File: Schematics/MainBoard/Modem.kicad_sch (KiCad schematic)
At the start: 27 parts, among them J10 Conn_02x05_Odd_Even, U13 ESP8266-01_ESP-01, U14 AMS1117-3.3, U15 TXS0102DCT, U16 ATmega644P-20A, Y1 ECS-3961-200-AU-TR

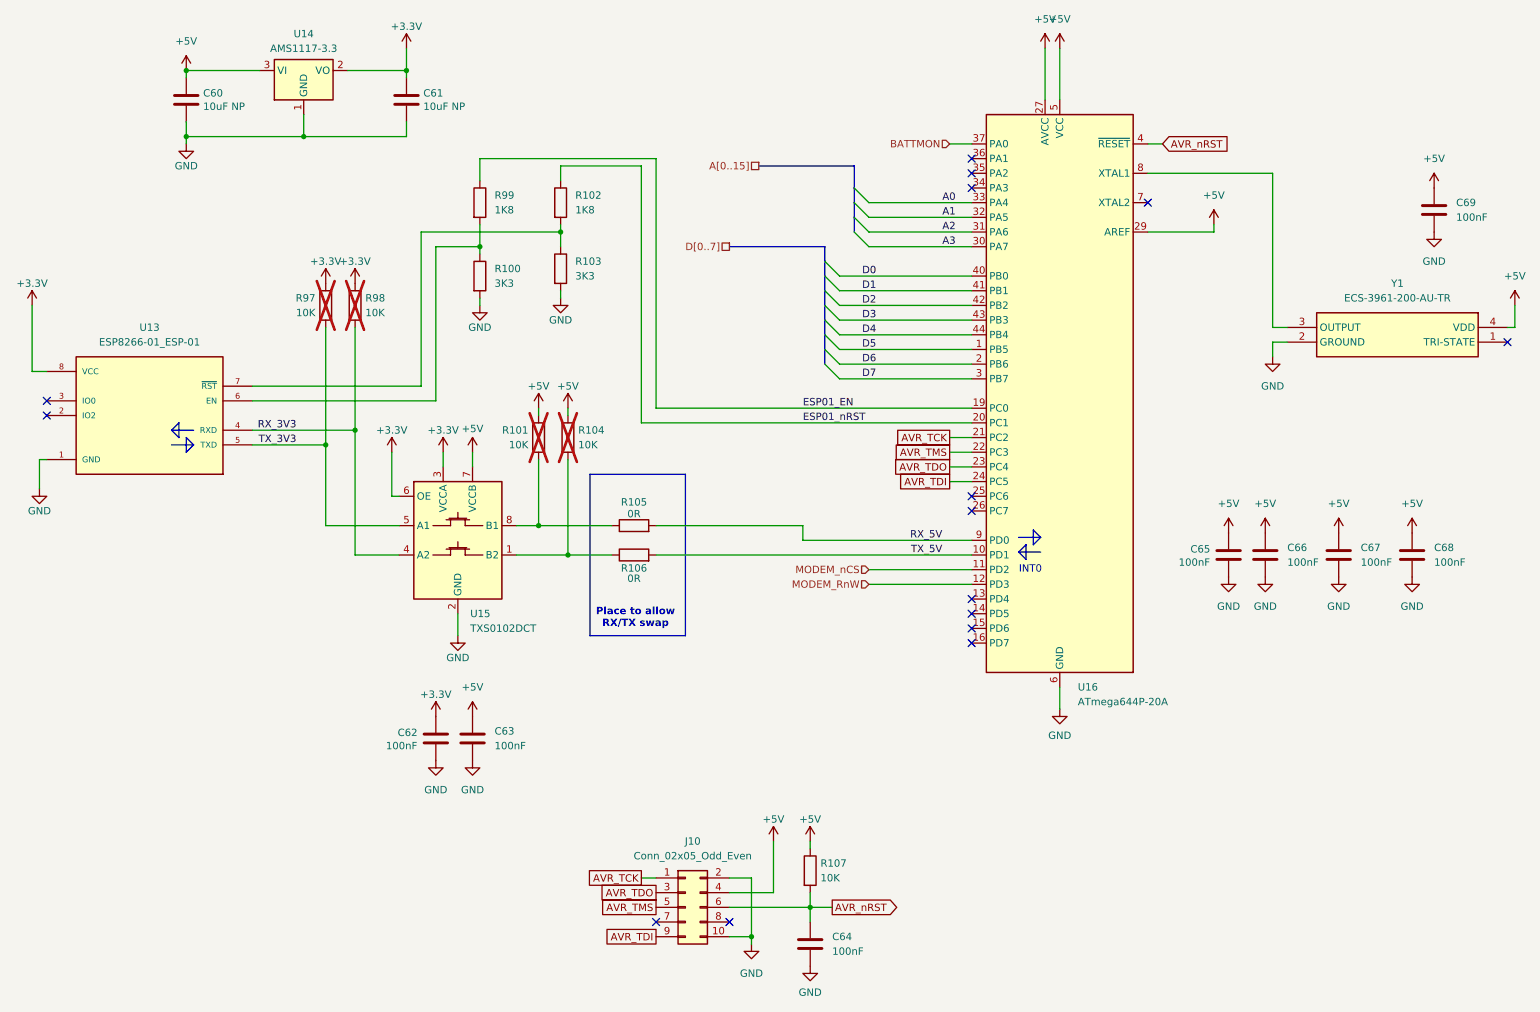
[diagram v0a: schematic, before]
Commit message: Move to a single board for everything (keyboard and main board)
Aim is to save height
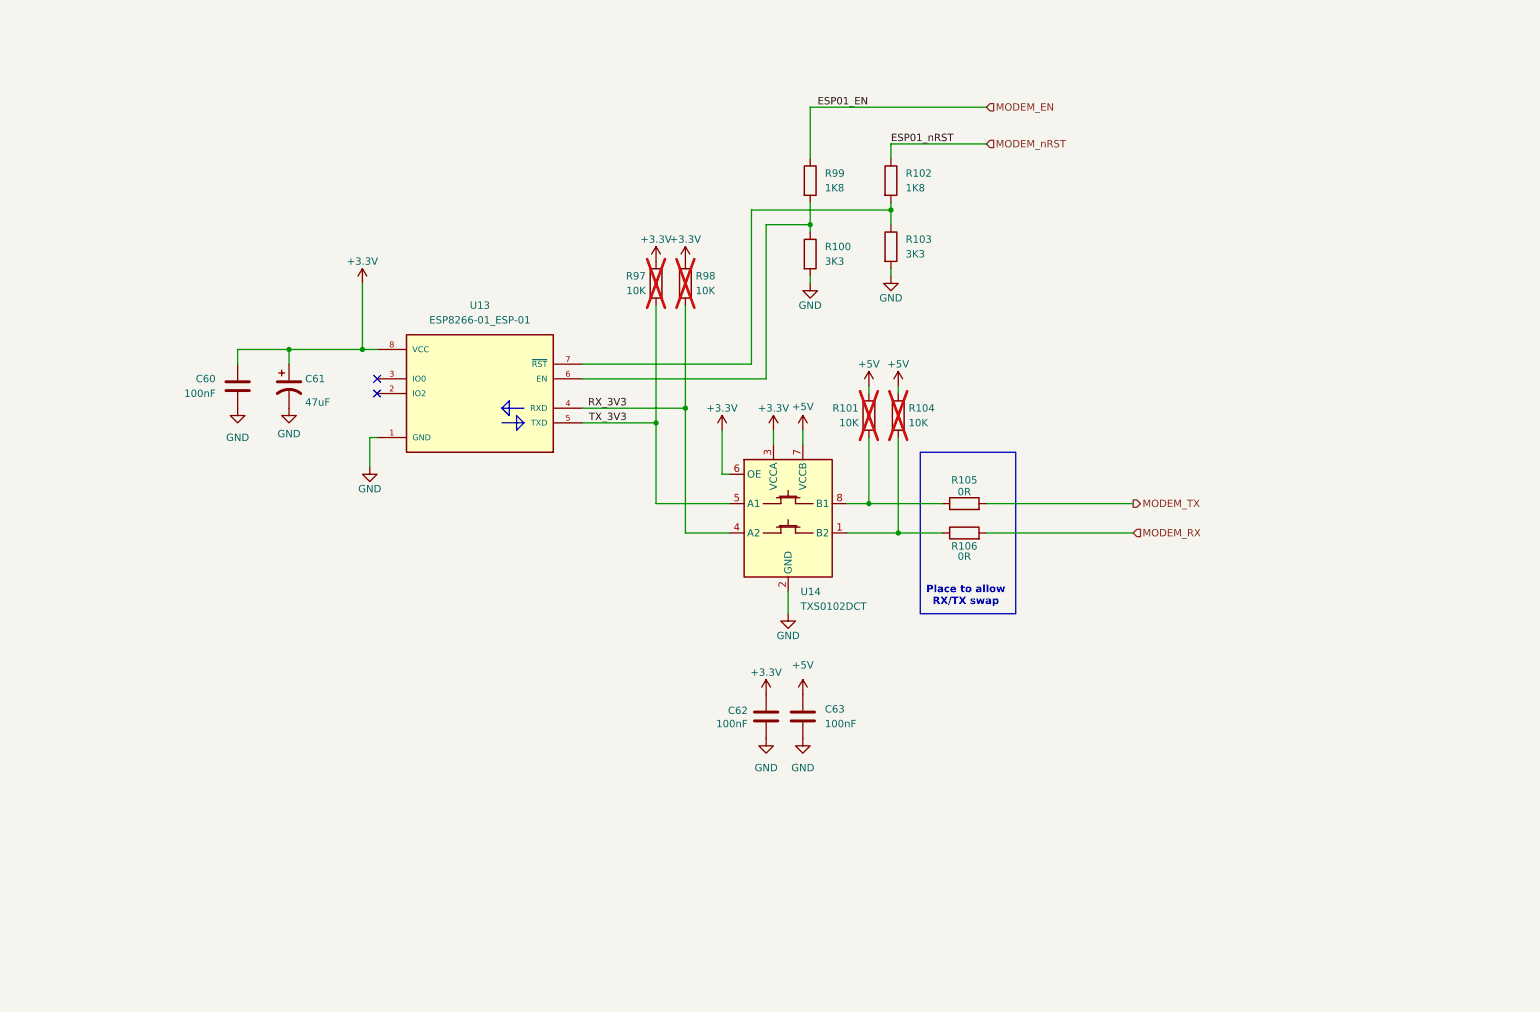
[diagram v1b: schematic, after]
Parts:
- removed C60, C61: 10uF NP, Capacitor_SMD:C_0805_2012Metric, symbol Device:C
- removed C64, C65, C66, C67, C69: 100nF, Capacitor_SMD:C_0402_1005Metric, symbol Device:C
- removed J10: Conn_02x05_Odd_Even, Connector_PinHeader_2.54mm:PinHeader_2x05_P2.54mm_Vertical, symbol Connector_Generic:Conn_02x05_Odd_Even
- removed R107: 10K, Resistor_SMD:R_0402_1005Metric, symbol Device:R
- removed U14: AMS1117-3.3, Package_TO_SOT_SMD:SOT-223-3_TabPin2, symbol Regulator_Linear:AMS1117-3.3
- removed U16: ATmega644P-20A, Package_QFP:TQFP-44_10x10mm_P0.8mm, symbol MCU_Microchip_ATmega:ATmega644P-20A
- removed Y1: ECS-3961-200-AU-TR, ECS-3961-200-AU-TR:ECS3961200AUTR, symbol ECS-3961-200-AU-TR:ECS-3961-200-AU-TR
- added C61: 47uF, Capacitor_SMD:C_1206_3216Metric, symbol Device:C_Polarized_US
- renumbered C68 to C60, U15 to U14
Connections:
- net +3.3V: now also C60.1, C61.1
- net +5V: no longer C60.1
- net GND: now also C61.2
- net ESP01_EN renamed MODEM_EN
- net ESP01_nRST renamed MODEM_nRST
- net RX_5V renamed MODEM_TX
- net TX_5V renamed MODEM_RX
- no-connect marks 15 -> 2
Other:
- note removed: "INT0"
- moved on the sheet: C60, C62, C63, R100, R101, R102, R103, R104, R105, R106, R97, R98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

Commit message: Work on PCB
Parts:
- R100, R102, R103, R99: footprint Resistor_SMD:R_0603_1608Metric -> Resistor_SMD:R_0402_1005Metric
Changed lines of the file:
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@@
 			)
 		)
-		(property "Footprint" "Resistor_SMD:R_0603_1608Metric"
+		(property "Footprint" "Resistor_SMD:R_0402_1005Metric"
 			(at 162.052 52.07 90)
 			(effects
@@
 			)
 		)
-		(property "Footprint" "Resistor_SMD:R_0603_1608Metric"
+		(property "Footprint" "Resistor_SMD:R_0402_1005Metric"
 			(at 148.082 64.77 90)
 			(effects
@@
 			)
 		)
-		(property "Footprint" "Resistor_SMD:R_0603_1608Metric"
+		(property "Footprint" "Resistor_SMD:R_0402_1005Metric"
 			(at 162.052 63.5 90)
 			(effects
@@
 			)
 		)
-		(property "Footprint" "Resistor_SMD:R_0603_1608Metric"
+		(property "Footprint" "Resistor_SMD:R_0402_1005Metric"
 			(at 148.082 52.07 90)
 			(effects

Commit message: Updates based on production files for JLC
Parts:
- C60, C62, C63: LCSC C113803 -> C307331
- R102, R99: LCSC C25890 -> C25871
- R105, R106: LCSC (none) -> C21189
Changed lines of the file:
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@@
 			)
 		)
-		(property "LCSC" "C113803"
+		(property "LCSC" "C307331"
 			(at 142.24 144.78 0)
 			(effects
@@
 			)
 		)
+		(property "LCSC" "C21189"
+			(at 176.53 107.95 90)
+			(effects
+				(font
+					(size 1.27 1.27)
+				)
+				(hide yes)
+			)
+		)
 		(pin "2"
 		)
@@
 			)
 		)
-		(property "LCSC" "C25890"
+		(property "LCSC" "C25871"
 			(at 163.83 52.07 0)
 			(effects
@@
 			)
 		)
-		(property "LCSC" "C113803"
+		(property "LCSC" "C307331"
 			(at 50.8 87.63 0)
 			(effects
@@
 			)
 		)
+		(property "LCSC" "C21189"
+			(at 176.53 113.03 90)
+			(effects
+				(font
+					(size 1.27 1.27)
+				)
+				(hide yes)
+			)
+		)
 		(pin "2"
 		)
@@
 			)
 		)
-		(property "LCSC" "C113803"
+		(property "LCSC" "C307331"
 			(at 148.59 144.78 0)
 			(effects
@@
 			)
 		)
-		(property "LCSC" "C25890"
+		(property "LCSC" "C25871"
 			(at 149.86 52.07 0)
 			(effects
